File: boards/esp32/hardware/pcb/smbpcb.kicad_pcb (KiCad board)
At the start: 2 copper layers, 85.4 x 70.4 mm, 66 parts, among them IC1 MiCS-6814, J1 USB_B_Micro, J2 PMS7003, Q1 SUD08P06-155L, SW1 RESET, SW2 RESET, U1 MCP73831-2-OT, U2 SGM6603-5.0YN6G_TR, U3 ESP32-WROOM-32, U4 SSD1306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

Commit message: moving stuff
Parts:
- U4: footprint mics:SSD1306_OLED-0.91-128x32 -> stuff:SSD1306_OLED-0.91-128x32
- moved AUX_CONN2 10.6 mm to (79.4, 96.3)
- moved AUX_CONN3 4.30 mm to (90.7, 96.3)
- moved AUX_CONN1 1.55 mm to (82.8, 76.8)
- moved EXT_BATT1 0.91 mm to (50.9, 40.8)
- moved BT1 0.77 mm to (50.8, 36.3)
- turned C6 to 180 degrees
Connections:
- U4 pad 1: Net-(U4-Pad1) -> Net-(C5-Pad1)
- U4 pad 12: Net-(U4-Pad12) -> Net-(R6-Pad2)
- U4 pad 13: Net-(U4-Pad13) -> Net-(C9-Pad2)
- U4 pad 14: +3V3 -> Net-(C10-Pad2)
- U4 pad 2: Net-(U4-Pad2) -> Net-(C5-Pad2)
- U4 pad 3: Net-(U4-Pad3) -> Net-(C6-Pad1)
- U4 pad 4: Net-(U4-Pad4) -> Net-(C6-Pad2)
- U4 pad 9: RES -> Net-(R2-Pad2)
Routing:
- net +3V3: track 226.0 -> 202.5 mm
- net RES: track 13.0 -> 0.00 mm
- net Net-(R2-Pad2): track 0.00 -> 13.0 mm
- net Net-(U4-Pad3): track 10.5 -> 0.00 mm
- net Net-(C6-Pad1): track 0.00 -> 10.5 mm
- net Net-(C10-Pad2): track 0.00 -> 8.53 mm
- net Net-(U4-Pad4): track 8.41 -> 0.00 mm
- net Net-(C6-Pad2): track 0.00 -> 8.41 mm
- net ESP_RX0: track 15.5 -> 7.72 mm
- net Net-(U4-Pad13): track 6.07 -> 0.00 mm
- net Net-(C9-Pad2): track 0.00 -> 6.07 mm
- net ESP_TX0: track 11.6 -> 5.63 mm
- net ESP_TX1: track 7.12 -> 1.66 mm
- net ESP_RX1: track 8.52 -> 4.36 mm
- net Net-(U4-Pad12): track 4.08 -> 0.00 mm
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
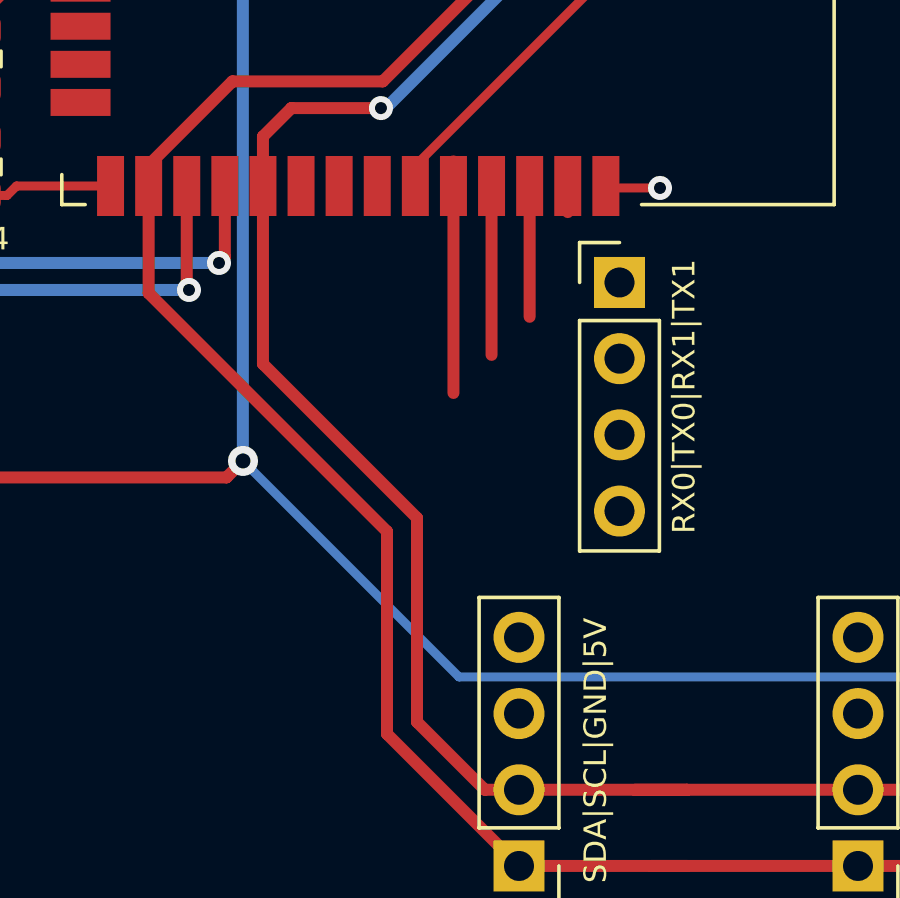
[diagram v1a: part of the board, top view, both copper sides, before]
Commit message: added status leds
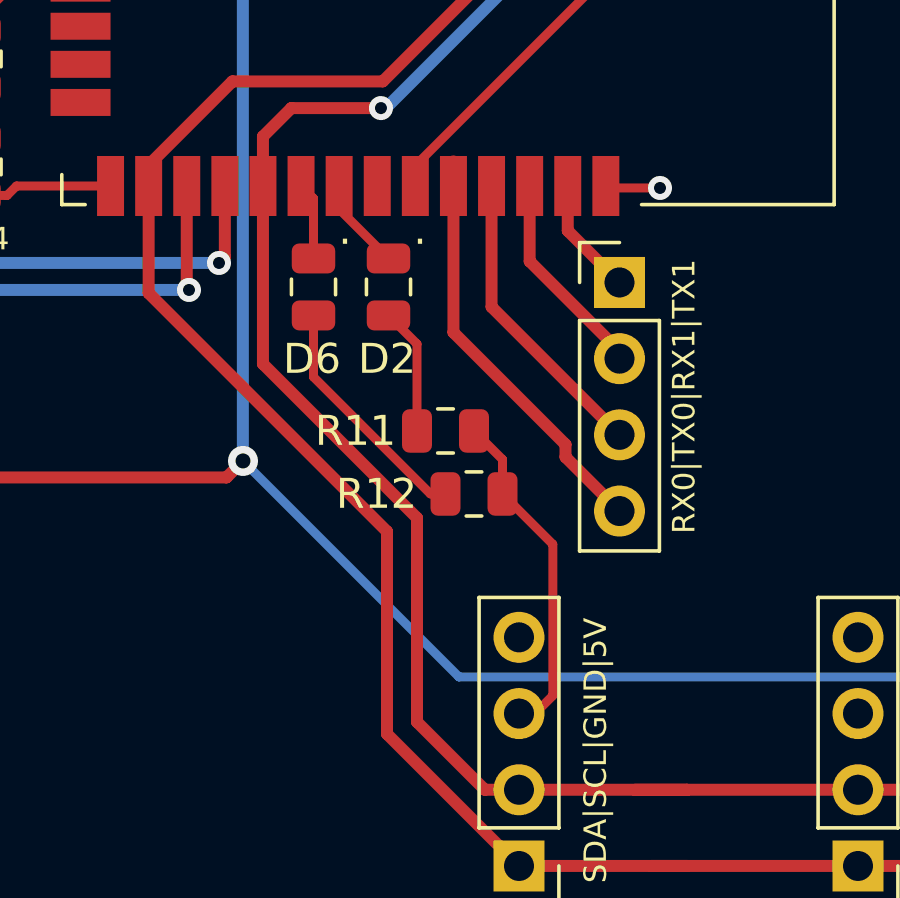
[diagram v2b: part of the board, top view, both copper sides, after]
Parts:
- added D2: LED_BLUE, Capacitor_SMD:C_0805_2012Metric, F.Cu at (75.0, 77.0)
- added D6: LED_GREEN, Capacitor_SMD:C_0805_2012Metric, F.Cu at (72.5, 77.0)
- added R11: 1k5, Capacitor_SMD:C_0805_2012Metric, F.Cu at (77.0, 81.8)
- added R12: 1k5, Capacitor_SMD:C_0805_2012Metric, F.Cu at (77.9, 83.9)
- R17, R18: value 4.7k -> 4k7
- R27: value 5.1k -> 5k1
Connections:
- U3 pad 30: unconnected-(U3-Pad30) -> LED_GREEN
- U3 pad 31: unconnected-(U3-Pad31) -> LED_BLUE
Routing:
- net GND: track 189.4 -> 200.7 mm
- net Net-(D6-Pad1): track 0.00 -> 8.07 mm
- net ESP_RX0: track 7.72 -> 13.9 mm
- net ESP_TX0: track 5.63 -> 10.1 mm
- net Net-(D2-Pad1): track 0.00 -> 4.24 mm
- net ESP_TX1: track 1.66 -> 5.59 mm
- net LED_BLUE: track 0.00 -> 3.10 mm
- net ESP_RX1: track 4.36 -> 7.00 mm
- net LED_GREEN: track 0.00 -> 2.59 mm

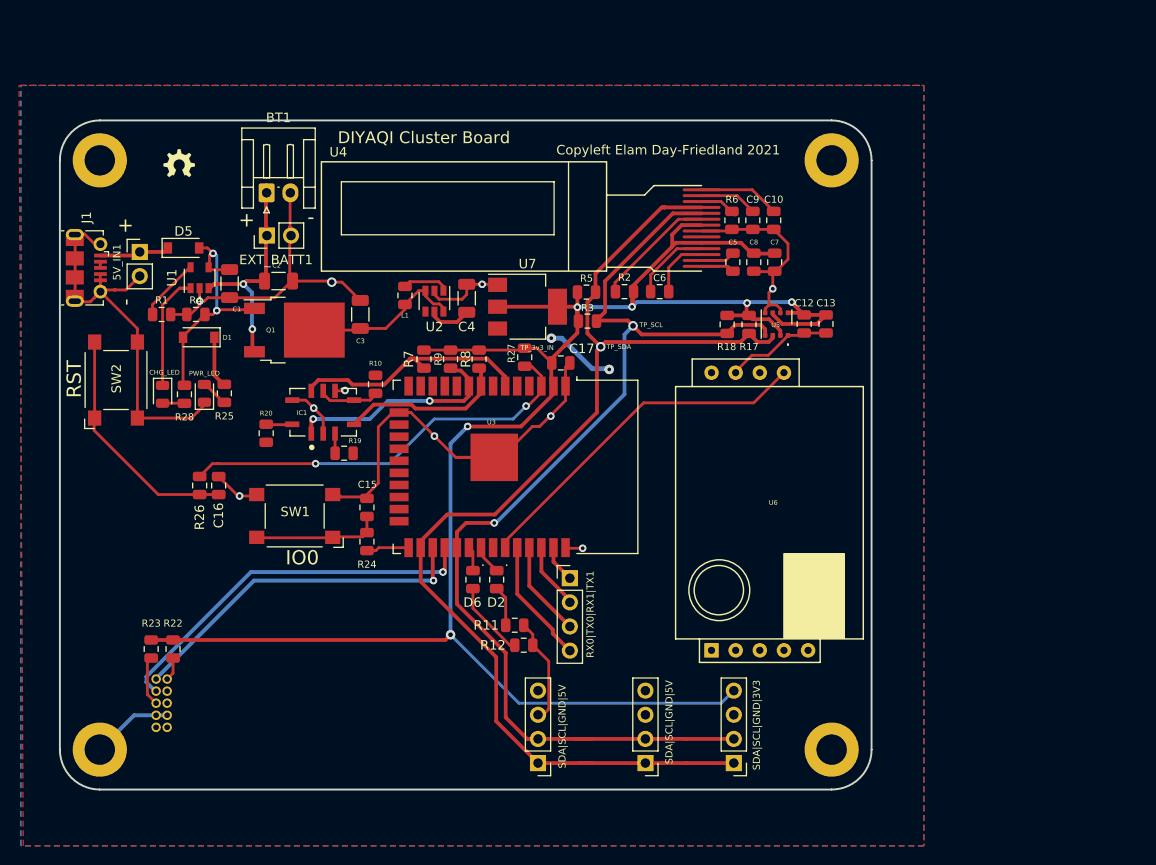
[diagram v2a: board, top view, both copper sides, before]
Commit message: changed some title block stuff
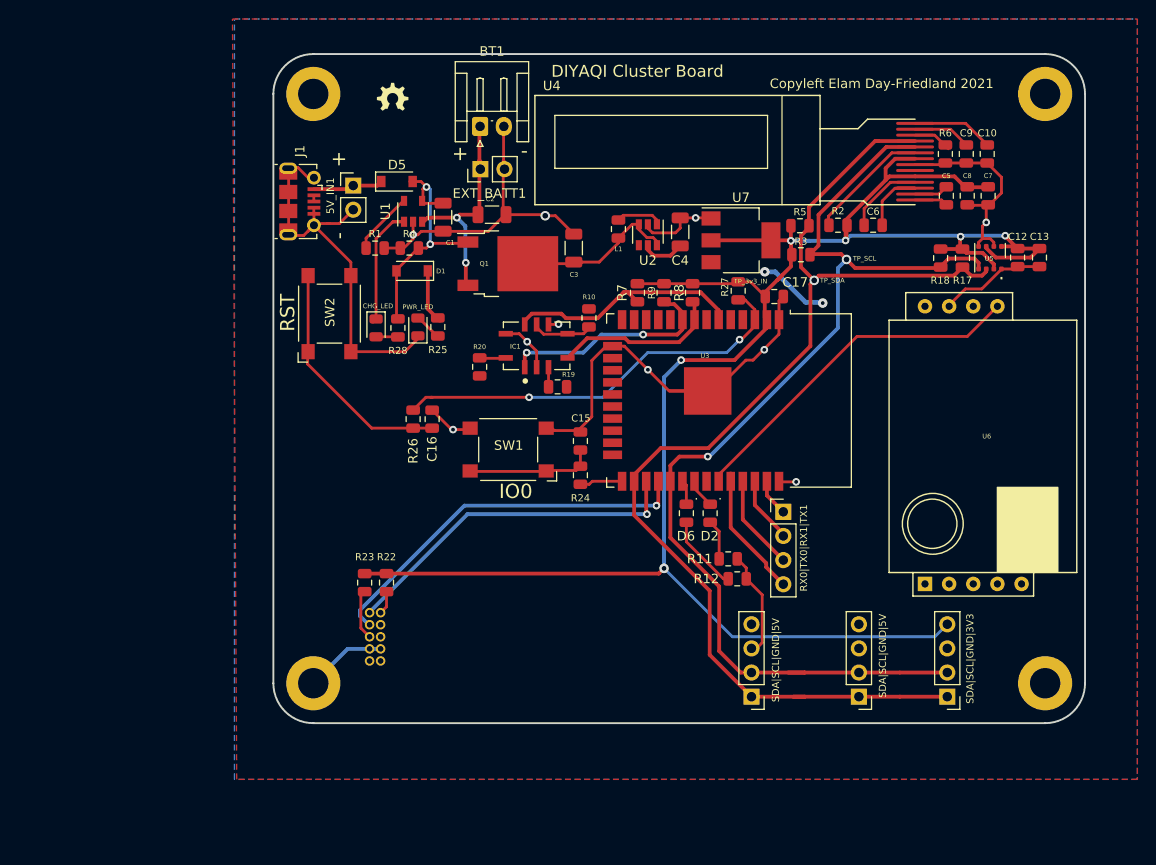
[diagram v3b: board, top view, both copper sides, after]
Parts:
- moved BT1 23.5 mm to (73.3, 29.3)
- moved C12 23.5 mm to (129.9, 43.1)
- moved C16 23.5 mm to (68.3, 60.1)
- moved C17 23.5 mm to (104.3, 47.2)
- moved C7 23.5 mm to (126.8, 36.6)
- moved C8 23.5 mm to (124.6, 36.6)
- moved D2 23.5 mm to (97.5, 70.0)
- moved D3 23.5 mm to (66.8, 50.4)
- moved D6 23.5 mm to (95.0, 70.0)
- moved R10 23.5 mm to (84.8, 49.5)
- moved R17 23.5 mm to (124.1, 43.2)
- moved R18 23.5 mm to (121.8, 43.2)
- moved R20 23.5 mm to (73.3, 54.6)
- moved R26 23.5 mm to (66.3, 60.1)
- moved R3 23.5 mm to (107.1, 42.8)
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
